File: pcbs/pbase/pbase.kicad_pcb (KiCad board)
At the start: 2 copper layers, 39 parts, among them J1 SD_Card, J2 Conn_01x04, J3 Conn_01x04, U1 LPCXpresso_LPC1769_revB, U2 acc_mpu9250_board, U3 GPS_EM506

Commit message: pbase edits
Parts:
- added G***: LOGO, footprints:logoUTN4, F.Cu at (122.4, 77.2)
- TP21: value TEST -> 5V
- TP22: value TEST -> 3V3
- moved REF** 115.6 mm to (202.7, 77.2)
- moved TP5 75.5 mm to (191.0, 105.2), turned to 90 degrees
- moved TP7 74.2 mm to (196.1, 105.2), turned to 90 degrees
- moved TP6 74.2 mm to (193.5, 105.2), turned to 270 degrees
- moved U3 73.7 mm to (193.0, 115.2)
- moved TP21 59.7 mm to (219.7, 53.3), turned to 0 degrees
- moved TP17 55.8 mm to (106.7, 101.1)
- moved TP22 55.0 mm to (214.6, 53.3), turned to 0 degrees
- moved TP20 54.8 mm to (114.3, 101.1)
- moved TP18 54.6 mm to (109.2, 101.1)
- moved TP19 50.8 mm to (111.8, 101.1)
- moved J3 47.1 mm to (214.6, 62.2), turned to 90 degrees
- moved J1 37.2 mm to (116.8, 127.5)
- moved R2 35.5 mm to (124.3, 109.7), turned to 0 degrees
- moved R3 35.0 mm to (105.3, 112.3), turned to 0 degrees
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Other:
- board outline added: 152.9 x 129.5 mm
- board text added: "Dice Ridolfi que para I2C como es lento no hay problema. Lo mismo pasa con SPI. USB Si trae problemas."
- board text added: "Grid: 20 mils para PLACING"
- board text added: "SD PLACING. VER PLACA INFOTRONIC Me gustaria que la entrada de esta SD quedara para el mismo lado que el lpc"
- board text removed: "Grid: THT 50 mils (checklsit)"

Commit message: PCB PLACING V1
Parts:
- added M3: MountingHole_3.2mm_M3, Mounting_Holes:MountingHole_3.2mm_M3, F.Cu at (228.6, 30.5)
- added M3: MountingHole_3.2mm_M3, Mounting_Holes:MountingHole_3.2mm_M3, F.Cu at (228.6, 137.2)
- added M3: MountingHole_3.2mm_M3, Mounting_Holes:MountingHole_3.2mm_M3, F.Cu at (86.4, 137.2)
- added M3: MountingHole_3.2mm_M3, Mounting_Holes:MountingHole_3.2mm_M3, F.Cu at (86.4, 30.5)
- added REF***: WEEE-Logo_5.6x8mm_SilkScreen, Symbols:WEEE-Logo_5.6x8mm_SilkScreen, F.Cu at (204.2, 83.3)
- J1: footprint Connectors:SD_Card_Receptacle -> footprints:SD_TE_2041021
- TP16: value CAP2.1 -> CAP2
- moved R6 92.9 mm to (219.8, 46.7), turned to 180 degrees
- moved R7 90.5 mm to (219.8, 49.3), turned to 180 degrees
- moved TP8 89.3 mm to (215.9, 63.0)
- moved TP9 89.3 mm to (218.4, 63.0)
- moved J2 89.1 mm to (215.9, 53.3)
- moved REF** 85.0 mm to (122.4, 105.2)
- moved R1 70.8 mm to (220.6, 118.4), turned to 180 degrees
- moved C2 64.8 mm to (158.8, 75.2)
- moved C1 64.4 mm to (158.8, 78.4)
- moved U1 63.8 mm to (160.0, 95.0)
- moved TP20 63.6 mm to (177.8, 105.1)
- moved TP1 63.6 mm to (221.0, 105.1)
- moved TP17 63.6 mm to (170.2, 105.1)
- moved TP18 63.6 mm to (172.7, 105.1)
- moved TP2 63.6 mm to (223.5, 105.1)
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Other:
- board size 152.9 x 129.5 mm -> 152.4 x 116.8 mm
- board text added: "1"
- board text added: "27"
- board text added: "28"
- board text added: "3v3"
- board text added: "54"
- board text added: "5V"
- board text added: "8"
- board text added: "9"
- board text added: "Alimentación"
- board text added: "GND"
- board text added: "LPC1769 Stick RevC / RevD"
- board text added: "MODULO CARGADOR DE BATERIA"
- board text added: "SD CARD"
- board text added: "TENGO QUE LLEGAR A 10 POR 12 CM"

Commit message: pcb replacing
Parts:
- removed the M3 at (228.6, 30.5)
- added REF**: MountingHole_3.2mm_M3_DIN965, Mounting_Holes:MountingHole_3.2mm_M3_DIN965, F.Cu at (228.6, 30.5)
- added REF**: MountingHole_3.2mm_M3_DIN965, Mounting_Holes:MountingHole_3.2mm_M3_DIN965, F.Cu at (138.2, 120.9)
- moved REF** 46.4 mm to (118.4, 151.4)
- moved J2 43.8 mm to (199.6, 12.7), turned to 180 degrees
- moved R7 42.1 mm to (223.0, 7.29), turned to 270 degrees
- moved R6 34.4 mm to (223.0, 12.5), turned to 90 degrees
- moved TP8 25.4 mm to (190.5, 63.0)
- moved R4 21.7 mm to (180.3, 87.9), turned to 270 degrees
- moved J3 21.3 mm to (183.9, 51.8)
- moved MOD1 16.8 mm to (198.4, 53.5)
- moved J1 16.6 mm to (147.0, 83.4)
- moved R5 14.9 mm to (173.2, 87.9), turned to 270 degrees
- moved C1 14.5 mm to (173.2, 79.7), turned to 270 degrees
- moved C2 9.90 mm to (162.6, 84.3), turned to 270 degrees
- moved R2 8.99 mm to (167.1, 87.9), turned to 270 degrees
- moved R3 8.74 mm to (167.1, 79.6), turned to 270 degrees
- moved U2 4.06 mm to (228.6, 110.2)
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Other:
- board size 152.4 x 116.8 mm -> 100 x 100 mm

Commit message: pcb fin 1
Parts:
- removed the M3 at (228.6, 137.2)
- removed the M3 at (86.4, 137.2)
- removed the M3 at (86.4, 30.5)
- removed REF**: GPS_em506, footprints:GPS_em506_size
- removed REF** (x2): MountingHole_3.2mm_M3_DIN965, Mounting_Holes:MountingHole_3.2mm_M3_DIN965
- removed REF***: WEEE-Logo_5.6x8mm_SilkScreen, Symbols:WEEE-Logo_5.6x8mm_SilkScreen
- removed TP21: 5V, footprints:TestPoint_THTPad_D1.5mm_Drill0.7mm
- removed TP22: 3V3, footprints:TestPoint_THTPad_D1.5mm_Drill0.7mm
- added F1: Fiducial_1mm_Dia_2.54mm_Outer_CopperTop, Fiducials:Fiducial_1mm_Dia_2.54mm_Outer_CopperTop, F.Cu at (189.0, 55.0)
- added F2: Fiducial_1mm_Dia_2.54mm_Outer_CopperTop, Fiducials:Fiducial_1mm_Dia_2.54mm_Outer_CopperTop, F.Cu at (111.0, 145.0)
- added G***: LOGO, footprints:logoUTN1, B.Cu at (183.7, 71.7)
- added GPS EM-506: Laird_Technologies_BMI-S-204-F_32.00x32.00mm, Shielding_Cabinets:Laird_Technologies_BMI-S-204-F_32.00x32.00mm, F.Cu at (147.9, 71.9)
- added M3: MountingHole_3.2mm_M3_DIN965, Mounting_Holes:MountingHole_3.2mm_M3_DIN965, F.Cu at (195.0, 55.0)
- added M3: MountingHole_3.2mm_M3_DIN965, Mounting_Holes:MountingHole_3.2mm_M3_DIN965, F.Cu at (152.0, 145.0)
- added M3: MountingHole_3.2mm_M3_DIN965, Mounting_Holes:MountingHole_3.2mm_M3_DIN965, F.Cu at (105.0, 145.0)
- added M3: MountingHole_3.2mm_M3_DIN965, Mounting_Holes:MountingHole_3.2mm_M3_DIN965, F.Cu at (105.0, 97.0)
- added M3: MountingHole_3.2mm_M3_DIN965, Mounting_Holes:MountingHole_3.2mm_M3_DIN965, F.Cu at (152.0, 97.0)
- added M3: MountingHole_3.2mm_M3_DIN965, Mounting_Holes:MountingHole_3.2mm_M3_DIN965, F.Cu at (105.0, 55.0)
- J1: footprint footprints:SD_TE_2041021 -> footprints:SD_TE_2041021_edit; moved to B.Cu
- moved R7 140.2 mm to (165.4, 135.1), turned to 180 degrees
- moved J2 137.9 mm to (160.0, 144.8), turned to 90 degrees
- moved R6 137.8 mm to (160.2, 135.1), turned to 0 degrees
- moved TP15 103.9 mm to (110.2, 88.9)
- moved TP13 96.5 mm to (120.4, 88.9)
- moved G*** 95.6 mm to (183.6, 71.7), turned to 0 degrees
- moved TP9 92.8 mm to (164.1, 138.2), turned to 0 degrees
- moved MOD1 91.7 mm to (107.0, 61.0), turned to 0 degrees
- moved TP14 89.2 mm to (122.9, 88.9)
- moved TP11 84.3 mm to (115.3, 88.9)
- moved TP10 84.3 mm to (117.9, 88.9)
- moved J3 83.4 mm to (155.0, 130.0), turned to 0 degrees
- moved TP8 80.6 mm to (161.5, 138.2), turned to 0 degrees
- moved TP16 79.5 mm to (112.8, 88.9), turned to 0 degrees
- moved TP12 79.5 mm to (125.5, 88.9)
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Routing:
- net +3V3: track 0.00 -> 346.1 mm, vias 0 -> 1
- net /Zigbee/RTS: track 0.00 -> 124.2 mm, vias 0 -> 1
- net /Zigbee/SLRQ: track 0.00 -> 123.4 mm
- net /Zigbee/RXD1: track 0.00 -> 115.7 mm, vias 0 -> 1
- net /Zigbee/TXD1: track 0.00 -> 112.9 mm
- net /Zigbee/SLEEP: track 0.00 -> 111.8 mm, vias 0 -> 1
- net /lpc1769/CAP2.1: track 0.00 -> 107.9 mm
- net /TarjetaSD/MOSI1: track 0.00 -> 100.1 mm, vias 0 -> 1
- net /TarjetaSD/MISO1: track 0.00 -> 98.2 mm, vias 0 -> 2
- net /TarjetaSD/SSEL1: track 0.00 -> 94.3 mm, vias 0 -> 1
- net +5V: track 0.00 -> 92.9 mm
- net /Zigbee/CTS: track 0.00 -> 92.0 mm, vias 0 -> 1
- net /TarjetaSD/SCK1: track 0.00 -> 91.2 mm
- net /Display/SDA2: track 0.00 -> 86.5 mm, vias 0 -> 1
- net /Display/SCL2: track 0.00 -> 81.5 mm, vias 0 -> 1
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- added copper zone on B.Cu, net GND
- added copper zone on F.Cu, net GND
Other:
- board text added: "DUDA: Puedo poner a parte de la SD los resistores en bottom?? Esto facilitaria el routeo"
- board text added: "GRID 20 MILS: - RES SMD - CAPS SMD - SD - TPs INTERMEDIOS EL RESTO CON 1MM"
- board text added: "M3"
- board text added: "SD PLACING. VER PLACA INFOTRONIC Me gustaria que la entrada de esta SD quedara para el mismo lado que el lpc. NECESITO UN FOOTPRINT!! AL QUE CONSEGUÍ LE FALTA UN PIN (13)"
- board text added: "correcto el tamaño de la VIA?"
- board text removed: "27"
- board text removed: "28"
- board text removed: "54"
- board text removed: "Alimentación"
- board text removed: "LPC1769 Stick RevC / RevD"
- board text removed: "MODULO CARGADOR DE BATERIA"
- board text removed: "SD CARD"
- board text removed: "SD PLACING. VER PLACA INFOTRONIC Me gustaria que la entrada de esta SD quedara para el mismo lado que el lpc"

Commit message: pbase pcb finalizado v1
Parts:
- removed the G*** at (183.6, 71.7)
- added REF**: logoUTN5, footprints:logoUTN5, F.Cu at (161.3, 92.7)
- added REF***: WEEE-Logo_5.6x8mm_SilkScreen, Symbols:WEEE-Logo_5.6x8mm_SilkScreen, F.Cu at (184.3, 93.2)
- moved F2 2.00 mm to (113.0, 145.0)
- moved F1 2.00 mm to (187.0, 55.0)
- moved CAP2 1.27 mm to (112.8, 87.6)
- moved CTS 1.27 mm to (125.5, 87.6)
- moved RTS 1.27 mm to (120.4, 87.6)
- moved RXD1 1.27 mm to (117.9, 87.6)
- moved SLEEP 1.27 mm to (122.9, 87.6)
- moved SLRQ 1.27 mm to (110.2, 87.6)
- moved TXD1 1.27 mm to (115.3, 87.6)
- moved G*** 0.84 mm to (183.9, 72.5)
- moved SCL2 0.38 mm to (164.1, 137.8)
- moved SDA2 0.38 mm to (161.5, 137.8)
- renumbered TP16 to CAP2, TP12 to CTS, TP7 to DIR, TP4 to FSYNC, TP3 to INT, TP18 to MISO1, TP17 to MOSI1, TP13 to RTS, TP10 to RXD1, TP6 to RXD3, TP19 to SCK1, TP2 to SCL0, TP9 to SCL2, TP1 to SDA0, TP8 to SDA2, TP14 to SLEEP, TP15 to SLRQ, TP20 to SSEL1, TP11 to TXD1, TP5 to TXD3
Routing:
- net /Zigbee/SLRQ: track 123.4 -> 115.7 mm
- net /Zigbee/SLEEP: track 111.8 -> 105.6 mm
- net /Zigbee/RTS: track 124.2 -> 118.9 mm
- net /lpc1769/CAP2.1: track 107.9 -> 105.7 mm
- net /TarjetaSD/data2: track 17.4 -> 16.2 mm
- net /Zigbee/TXD1: track 112.9 -> 113.8 mm, vias 0 -> 1
- net +5V: track 92.9 -> 92.3 mm
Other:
- board text added: ".B"
- board text added: "10"
- board text added: "5v"
- board text added: "ACC"
- board text added: "Assy:"
- board text added: "DUDA: - Puedo poner a parte de la SD los resistores en bottom?? Esto facilitaria el routeo y reduciria el uso de vias. - Las vias que use ahí están bien? Traería problemas?"
- board text added: "DUDA: COMO PONER VIAS EN PARALELO?"
- board text added: "DUDA: Es correcta la forma en la que conecte ssel1 a traves de la via?"
- board text added: "DUDA: correcto el tamaño de la VIA?"
- board text added: "Display"
- board text added: "GPS"
- board text added: "LPCXpresso LPC1769"
- board text added: "Medidor de posición y velocidad de sujetos en movimiento."
- board text added: "N°:"
- board text added: "PLACA BASE"
- board text added: "POWER"
- board text added: "PROYECTO 4TO"
- board text added: "Rev C, Rev D"
- board text added: "SD"
- board text added: "SD CARD"
- board text added: "U"
- board text added: "UT"
- board text added: "V1.01"
- board text added: "versión"
- board text added: "© Alegre M.E., Bautista L, Tarazona L. 2018"
- board text removed: "DUDA: Puedo poner a parte de la SD los resistores en bottom?? Esto facilitaria el routeo"
- board text removed: "SD PLACING. VER PLACA INFOTRONIC Me gustaria que la entrada de esta SD quedara para el mismo lado que el lpc. NECESITO UN FOOTPRINT!! AL QUE CONSEGUÍ LE FALTA UN PIN (13)"
- board text removed: "TENGO QUE LLEGAR A 10 POR 12 CM"
- board text removed: "correcto el tamaño de la VIA?"

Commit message: pcb finalizado
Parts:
- added G***: LOGO, footprints:logoGIBIO, F.Cu at (136.9, 127.6)
- added G***: LOGO, footprints:logoGIBIO5, F.Cu at (141.5, 127.0)
- J1: moved to F.Cu
- moved C1 40.8 mm to (121.9, 102.6), turned to 270 degrees
- moved C2 38.8 mm to (125.0, 102.6), turned to 270 degrees
- moved R3 37.3 mm to (128.0, 102.6), turned to 270 degrees
- moved R2 17.4 mm to (140.5, 102.6), turned to 270 degrees
- moved R4 14.5 mm to (137.7, 102.6), turned to 270 degrees
- moved R5 12.1 mm to (134.6, 102.6), turned to 270 degrees
- moved SDA2 8.25 mm to (161.5, 129.5)
- moved J2 7.62 mm to (160.3, 137.2)
- moved R7 7.06 mm to (162.8, 141.7), turned to 90 degrees
- moved R6 6.56 mm to (160.3, 141.7), turned to 90 degrees
- moved SCL2 6.25 mm to (161.5, 132.1)
- moved DIR 5.08 mm to (161.5, 116.8)
- moved TXD3 5.08 mm to (161.5, 111.8)
- moved J1 3.56 mm to (113.8, 124.5), turned to 270 degrees
- moved REF*** 0.92 mm to (183.4, 93.5)
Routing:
- net +3V3: track 346.1 -> 274.5 mm, vias 1 -> 0
- net /TarjetaSD/data2: track 16.2 -> 43.9 mm, vias 1 -> 0
- net /TarjetaSD/MISO1: track 98.3 -> 85.1 mm, vias 2 -> 1
- net /acc/FSYNC: track 39.3 -> 28.8 mm
- net /TarjetaSD/SSEL1: track 94.3 -> 102.5 mm
- net /GPS/TXD3: track 70.7 -> 63.1 mm, vias 0 -> 1
- net /Zigbee/RXD1: track 115.3 -> 121.1 mm
- net /Zigbee/TXD1: track 113.8 -> 118.4 mm
- net /TarjetaSD/SCK1: track 91.2 -> 86.8 mm, vias 0 -> 1
- net /lpc1769/CAP2.1: track 105.7 -> 110.0 mm, vias 0 -> 1
- net /GPS/RXD3: track 68.3 -> 64.2 mm, vias 0 -> 1
- net Net-(J1-Pad13): track 49.7 -> 53.8 mm
- net /GPS/DIR: track 63.5 -> 67.2 mm, vias 0 -> 1
- net /Zigbee/CTS: track 92.2 -> 95.6 mm
- net /Display/SDA2: track 86.0 -> 83.4 mm, vias 1 -> 0
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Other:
- board text added: "PER4MANCE"
- board text added: "V1.02"
- board text added: "▶"
- board text removed: "10"
- board text removed: "DUDA: Es correcta la forma en la que conecte ssel1 a traves de la via?"
- board text removed: "V1.01"

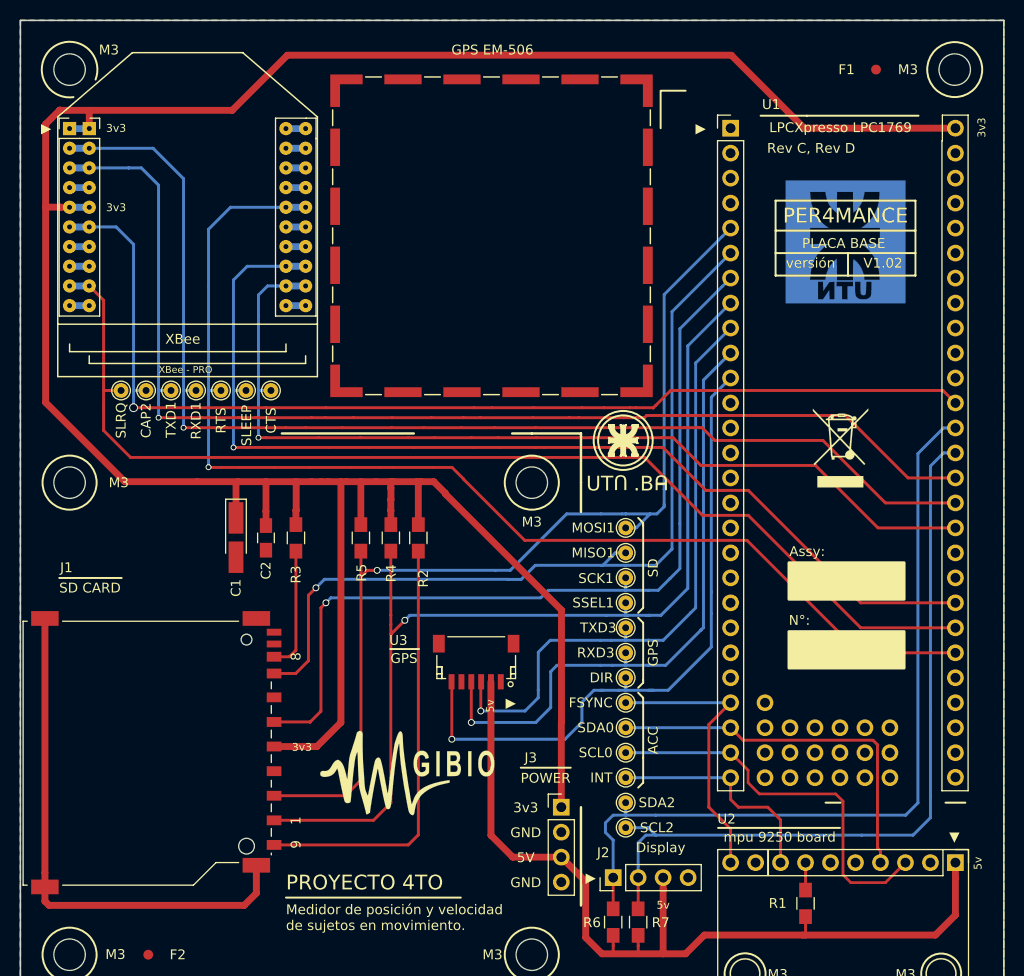
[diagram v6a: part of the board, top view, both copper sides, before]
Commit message: PCB correcion pista 3V3
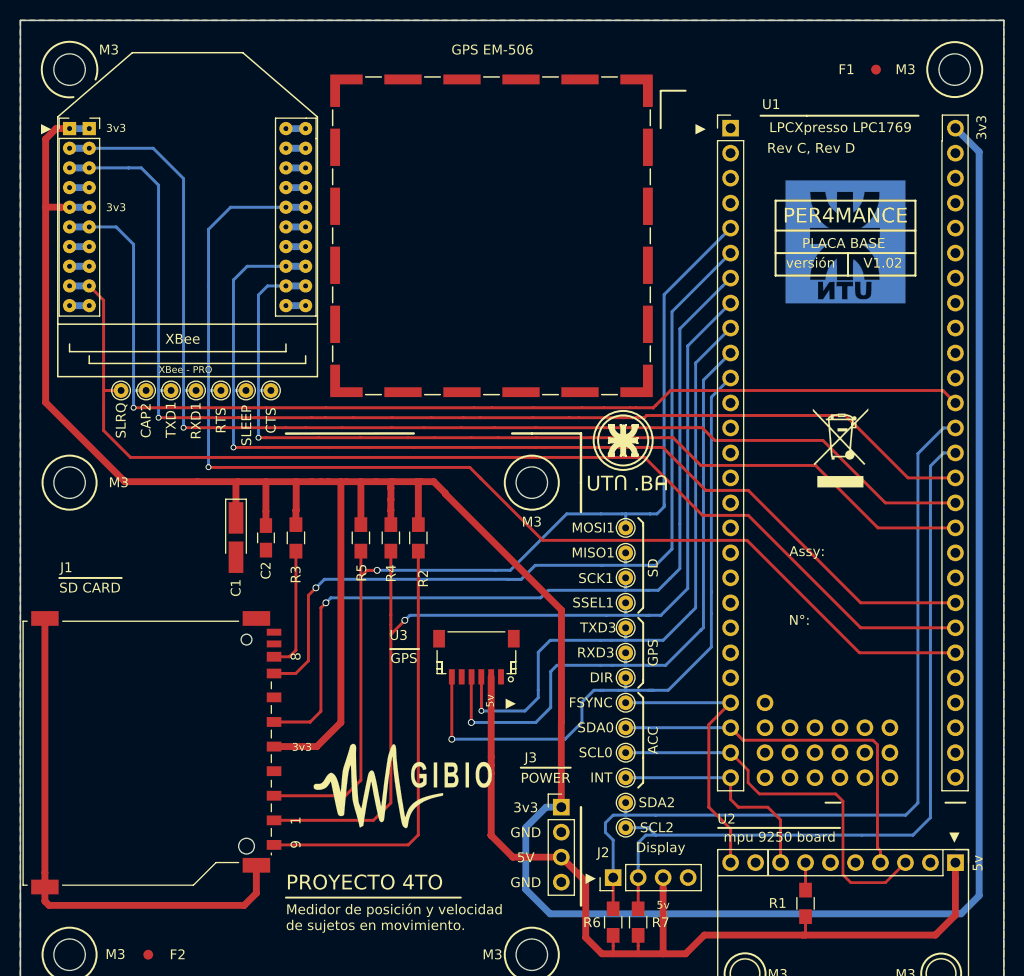
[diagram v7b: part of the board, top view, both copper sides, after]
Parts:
- moved G*** 1.48 mm to (136.2, 128.9)
- moved G*** 1.17 mm to (141.2, 128.1)
- moved U3 0.50 mm to (146.4, 114.8)
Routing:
- net +3V3: track 274.5 -> 313.1 mm
- net /TarjetaSD/MOSI1: track 100.8 -> 99.1 mm
- net /TarjetaSD/MISO1: track 85.1 -> 83.5 mm
- net /GPS/TXD3: track 63.1 -> 64.1 mm
- net /GPS/RXD3: track 64.2 -> 64.8 mm
- net +5V: track 91.5 -> 92.0 mm
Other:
- board text added: "Material: FR4"
- board text removed: "DUDA: COMO PONER VIAS EN PARALELO?"

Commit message: PLACA FINALIZADA
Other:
- board text added: "Material: FR4 Copper Weight: 1oz / 35um PCB SIZE: 100 X 100 mm PCB COLOR: RED"
- board text removed: "Material: FR4"
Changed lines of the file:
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@@
 (kicad_pcb (version 4) (host pcbnew 4.0.7-e2-6376~58~ubuntu16.04.1)
   (general
-    (links 0)
-    (no_connects 0)
+    (links 99)
+    (no_connects 14)
     (area 99.924999 49.924999 200.075001 150.075001)
     (thickness 1.6)
@@
     (pad_drill 3.2)
     (pad_to_mask_clearance 0.2)
-    (aux_axis_origin 0 0)
+    (aux_axis_origin 120 145)
     (visible_elements 7FFFFFFF)
     (pcbplotparams
@@
     (pad 1 np_thru_hole circle (at 0 0) (size 3.2 3.2) (drill 3.2) (layers *.Cu *.Mask))
   )
-  (gr_text "Material: FR4" (at 228 60) (layer Cmts.User)
-    (effects (font (size 1.5 1.5) (thickness 0.3)))
+  (gr_text "Material: FR4\nCopper Weight: 1oz / 35um\nPCB SIZE: 100 X 100 mm\nPCB COLOR: RED\n" (at 220 60) (layer Cmts.User)
+    (effects (font (size 1.5 1.5) (thickness 0.3)) (justify left))
   )
   (dimension 3.2 (width 0.3) (layer Dwgs.User)
@@
     (effects (font (size 1.5 1.5) (thickness 0.3)) (justify left))
   )
-  (gr_text "© Alegre M.E., Bautista L, Tarazona L. 2018\n" (at 130.048 148.336) (layer B.Cu)
-    (effects (font (size 1 1) (thickness 0.25)) (justify mirror))
+  (gr_text "© Alegre M.E., \nBautista L, \nTarazona L. \n2018\n" (at 145 140) (layer B.Cu)
+    (effects (font (size 1.5 1.5) (thickness 0.3)) (justify left mirror))
   )
   (gr_text "© Alegre M.E., Bautista L, Tarazona L. 2018\n" (at 129.413 148.336) (layer F.SilkS)
